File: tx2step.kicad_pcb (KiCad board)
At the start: 2 copper layers, 86.4 x 31.8 mm, 64 parts, among them CON1 BARREL_JACK, IC1 TPS2113A, IC2 MCP73831, IC3 TPS61202, IC4 DRV8834, IC5 DRV8834, J1 Prog, J2 8P8C, J3 CHASSIS_SWITCHES, J4 6P4Cx2, SW1 SW_DIP_x02, U1 ATmega328P-MMH, Y1 16 MHz

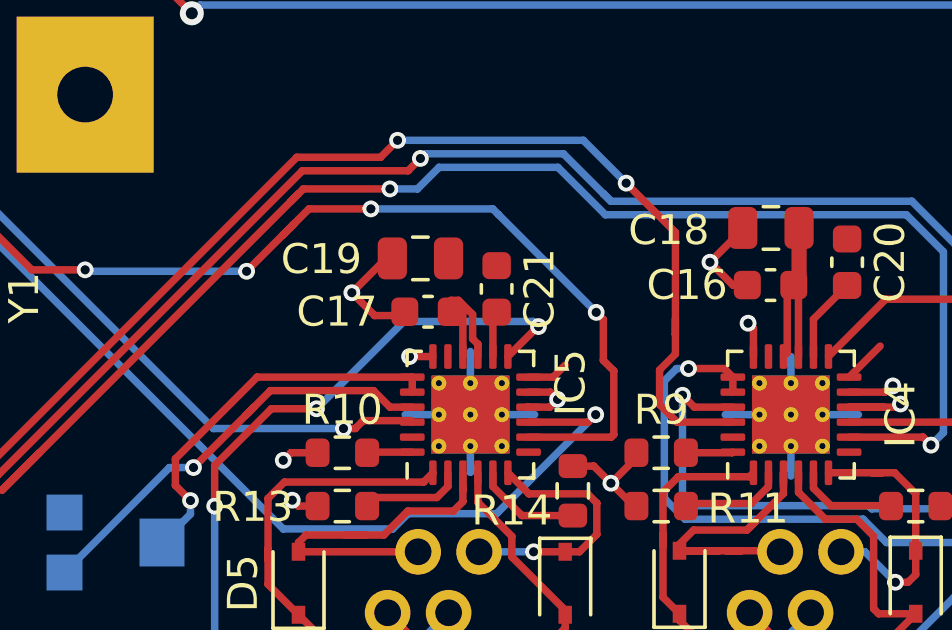
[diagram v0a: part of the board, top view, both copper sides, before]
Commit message: Restore capacitors on DRV8834 VINT
This pin still needs a capacitor even if it's not being used to
supply the CONFIG pin.
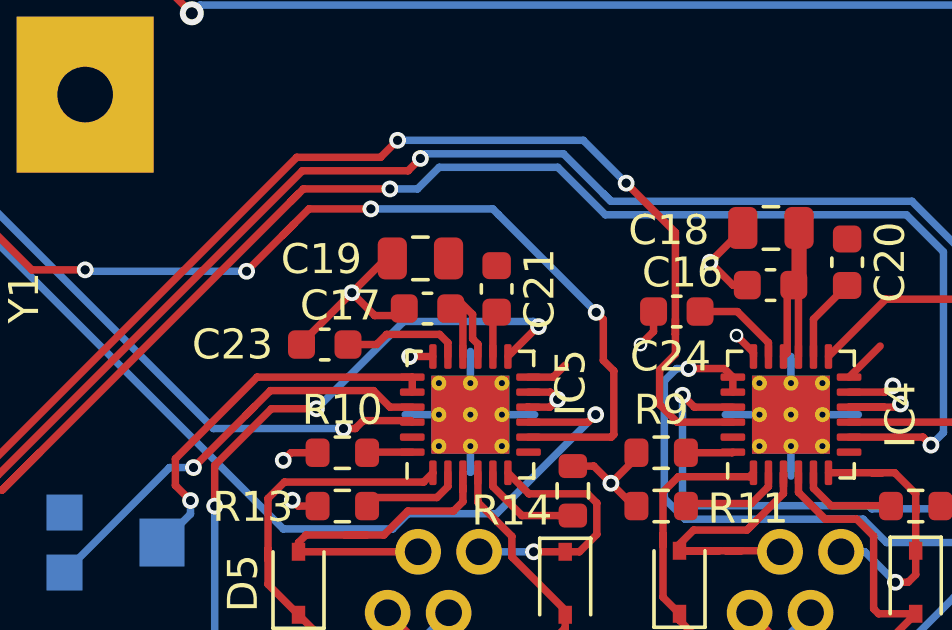
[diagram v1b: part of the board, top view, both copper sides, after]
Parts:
- added C23: 2.2 µF, Capacitor_SMD:C_0603_1608Metric, F.Cu at (140.6, 69.8)
- added C24: 2.2 µF, Capacitor_SMD:C_0603_1608Metric, F.Cu at (152.3, 68.7)
- moved C17 0.11 mm to (144.0, 68.6)
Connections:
- IC4 pad 17: (no net) -> Net-(C24-Pad2)
- IC4 pad 23: (no net) -> Net-(IC4-Pad23)
- IC4 pad 7: (no net) -> Net-(IC4-Pad7)
- IC5 pad 17: (no net) -> Net-(C23-Pad2)
- IC5 pad 23: (no net) -> Net-(IC5-Pad23)
- IC5 pad 7: (no net) -> Net-(IC5-Pad7)
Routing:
- net Net-(C23-Pad2): track 0.00 -> 4.05 mm
- net GND: track 102.9 -> 106.3 mm, vias 46 -> 47
- net Net-(C24-Pad2): track 0.00 -> 3.17 mm

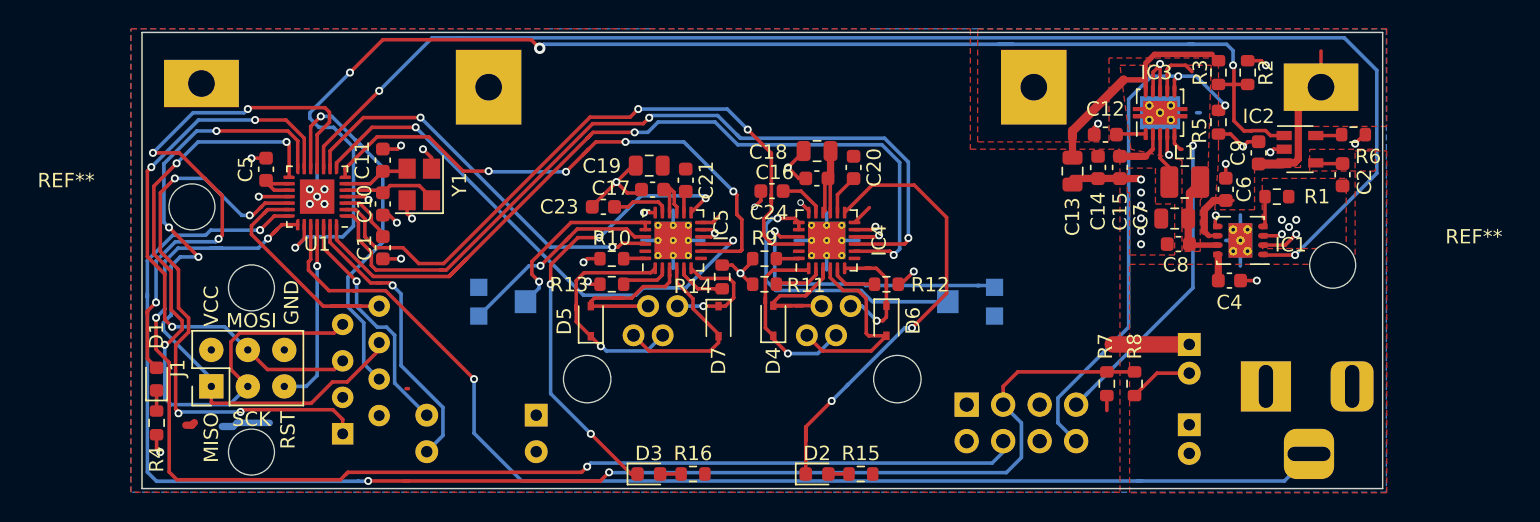
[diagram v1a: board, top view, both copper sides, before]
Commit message: Delete driver error LEDs
They don't actually seem particularly useful
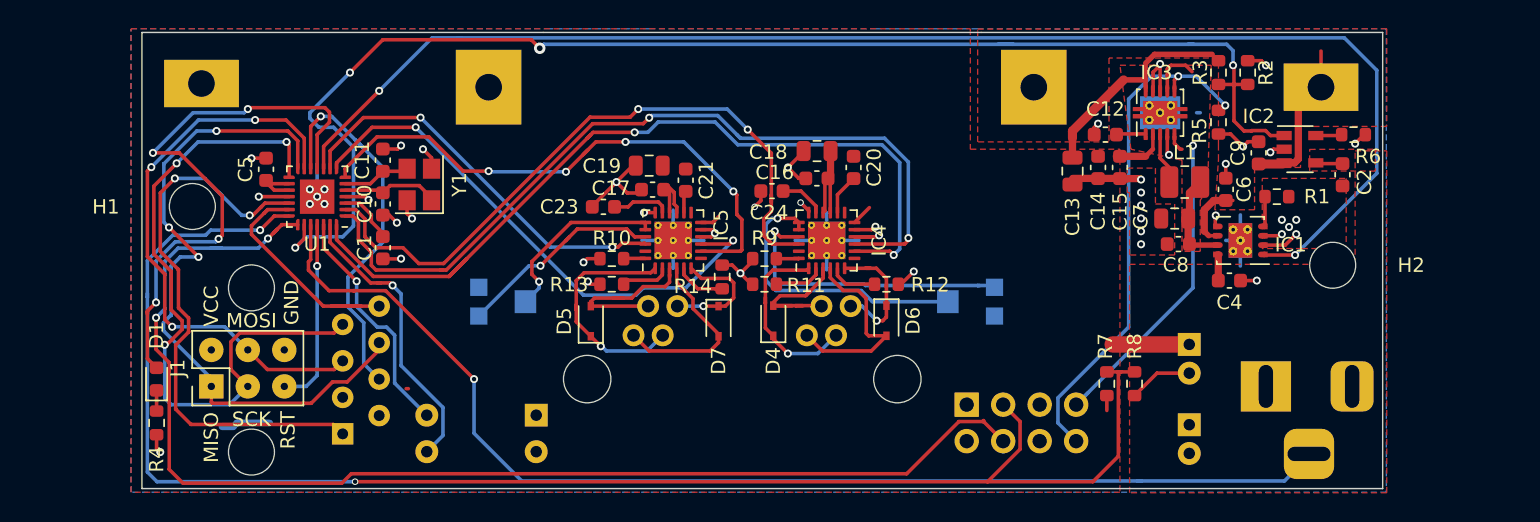
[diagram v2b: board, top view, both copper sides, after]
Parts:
- removed D2: ERR_RA, LED_SMD:LED_0603_1608Metric
- removed D3: ERR_DEC, LED_SMD:LED_0603_1608Metric
- removed R15, R16: 470Ω, Resistor_SMD:R_0603_1608Metric
- removed REF** (x2): MountingHole_3.2mm_M3, MountingHole:MountingHole_3.2mm_M3
- added H1: MountingHole, MountingHole:MountingHole_3.2mm_M3, F.Cu at (112.0, 69.8)
- added H2: MountingHole, MountingHole:MountingHole_3.2mm_M3, F.Cu at (191.3, 73.9)
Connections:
- IC4 pad 13: Net-(D2-Pad1) -> (no net)
- IC4 pad 23: Net-(IC4-Pad23) -> (no net)
- IC4 pad 7: Net-(IC4-Pad7) -> (no net)
- IC5 pad 13: Net-(D3-Pad1) -> (no net)
- IC5 pad 23: Net-(IC5-Pad23) -> (no net)
- IC5 pad 7: Net-(IC5-Pad7) -> (no net)
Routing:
- net Net-(D2-Pad1): track 32.6 -> 0.00 mm, vias 2 -> 0
- net Net-(D3-Pad1): track 31.6 -> 0.00 mm, vias 4 -> 0
- net /TRACK_RATE: track 103.3 -> 109.3 mm, vias 3 -> 2
- net Net-(D3-Pad2): track 1.46 -> 0.00 mm
- net /GUIDE_RATE: track 86.8 -> 88.2 mm, vias 3 -> 2
- net Net-(D2-Pad2): track 1.44 -> 0.00 mm
- net /JS_RA: track 40.6 -> 39.8 mm, vias 4 -> 2
- net VCC: track 48.8 -> 48.2 mm

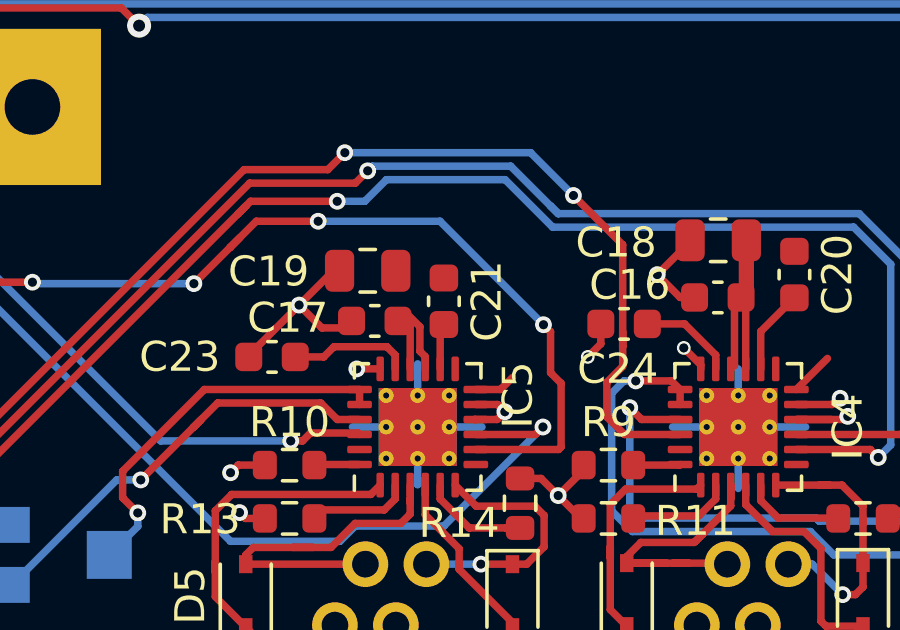
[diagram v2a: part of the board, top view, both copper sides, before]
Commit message: fix minor clearance issues
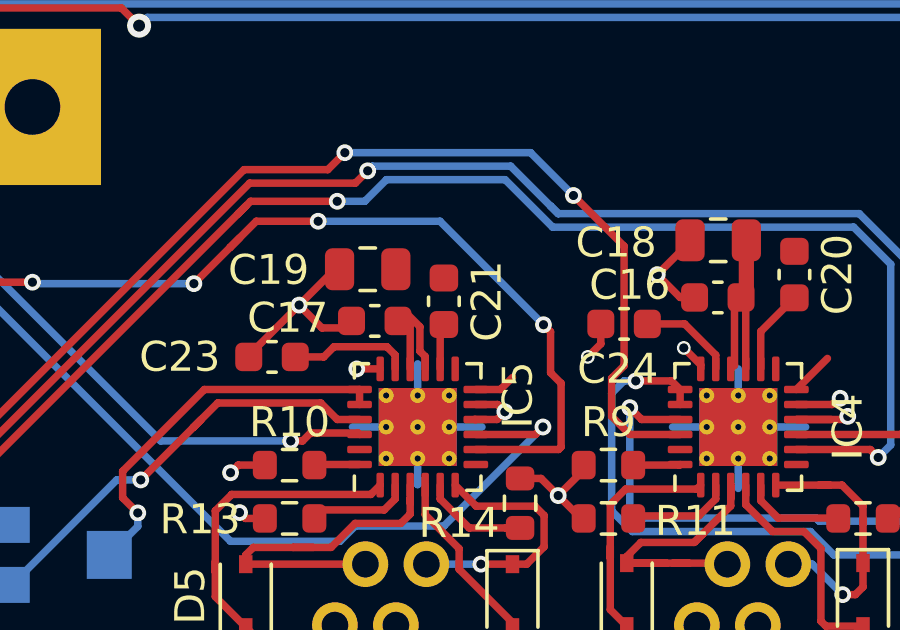
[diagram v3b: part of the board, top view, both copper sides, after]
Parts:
- moved C19 0.05 mm to (143.8, 66.9)
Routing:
- net /RA_PWR: track 46.8 -> 46.1 mm
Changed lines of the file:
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@@
     (thickness 1.6)
     (drawings 36)
-    (tracks 874)
+    (tracks 872)
     (zones 0)
     (modules 62)
@@
   )
   (module Capacitor_SMD:C_0805_2012Metric (layer F.Cu)
-    (at 143.764 66.929 180)
+    (at 143.764 66.8782 180)
     (descr "Capacitor SMD 0805 (2012 Metric), square (rectangular) end terminal, IPC_7351 nominal, (Body size source: https://docs.google.com/spreadsheets/d/1BsfQQcO9C6DZCsRaXUlFlo91Tg2WpOkGARC1WS5S8t0/edit?usp=sharing), generated with kicad-footprint-generator")
     (tags capacitor)
@@
   (via (at 143.002 62.992) (size 0.5588) (drill 0.3048) (layers F.Cu B.Cu) (net 23))
   (segment (start 143.002 62.992) (end 149.1944 62.992) (width 0.25) (layer B.Cu) (net 23))
-  (segment (start 154.178 72.386) (end 152.32241 72.386) (width 0.25) (layer F.Cu) (net 23) (status 10))
-  (segment (start 152.32241 72.386) (end 151.73641 71.8) (width 0.25) (layer F.Cu) (net 23))
-  (segment (start 151.73641 70.646104) (end 152.26359 70.118924) (width 0.25) (layer F.Cu) (net 23))
-  (segment (start 151.73641 71.8) (end 151.73641 70.646104) (width 0.25) (layer F.Cu) (net 23))
   (segment (start 143.002 62.992) (end 142.43601 63.55799) (width 0.25) (layer F.Cu) (net 23))
   (segment (start 142.43601 63.55799) (end 139.642009 63.557991) (width 0.25) (layer F.Cu) (net 23))
   (via (at 150.622 64.4196) (size 0.5588) (drill 0.3048) (layers F.Cu B.Cu) (net 23))
   (segment (start 149.1944 62.992) (end 150.622 64.4196) (width 0.25) (layer B.Cu) (net 23))
-  (segment (start 150.622 64.4196) (end 152.26359 66.06119) (width 0.25) (layer F.Cu) (net 23))
-  (segment (start 152.26359 66.06119) (end 152.26359 69.45959) (width 0.25) (layer F.Cu) (net 23))
-  (segment (start 152.26359 70.118924) (end 152.26359 69.45959) (width 0.25) (layer F.Cu) (net 23))
-  (segment (start 152.26359 69.45959) (end 152.26359 68.95159) (width 0.25) (layer F.Cu) (net 23))
   (segment (start 139.642009 63.557991) (end 129.456 73.744) (width 0.25) (layer F.Cu) (net 23))
   (segment (start 129.456 73.744) (end 127.724514 73.744) (width 0.25) (layer F.Cu) (net 23))
   (segment (start 126.624514 72.644) (end 124.744166 72.644) (width 0.25) (layer F.Cu) (net 23))
   (segment (start 127.724514 73.744) (end 126.624514 72.644) (width 0.25) (layer F.Cu) (net 23))
+  (segment (start 152.501086 72.386) (end 154.178 72.386) (width 0.25) (layer F.Cu) (net 23))
+  (segment (start 151.895599 71.780513) (end 152.501086 72.386) (width 0.25) (layer F.Cu) (net 23))
+  (segment (start 151.895599 70.509887) (end 151.895599 71.780513) (width 0.25) (layer F.Cu) (net 23))
+  (segment (start 152.31 70.095486) (end 151.895599 70.509887) (width 0.25) (layer F.Cu) (net 23))
+  (segment (start 152.31 66.1076) (end 152.31 70.095486) (width 0.25) (layer F.Cu) (net 23))
+  (segment (start 150.622 64.4196) (end 152.31 66.1076) (width 0.25) (layer F.Cu) (net 23))
   (segment (start 143.4925 71.386) (end 143.4925 70.886) (width 0.25) (layer F.Cu) (net 24) (status 30))
   (via (at 136.1 75) (size 0.5588) (drill 0.3048) (layers F.Cu B.Cu) (net 24))

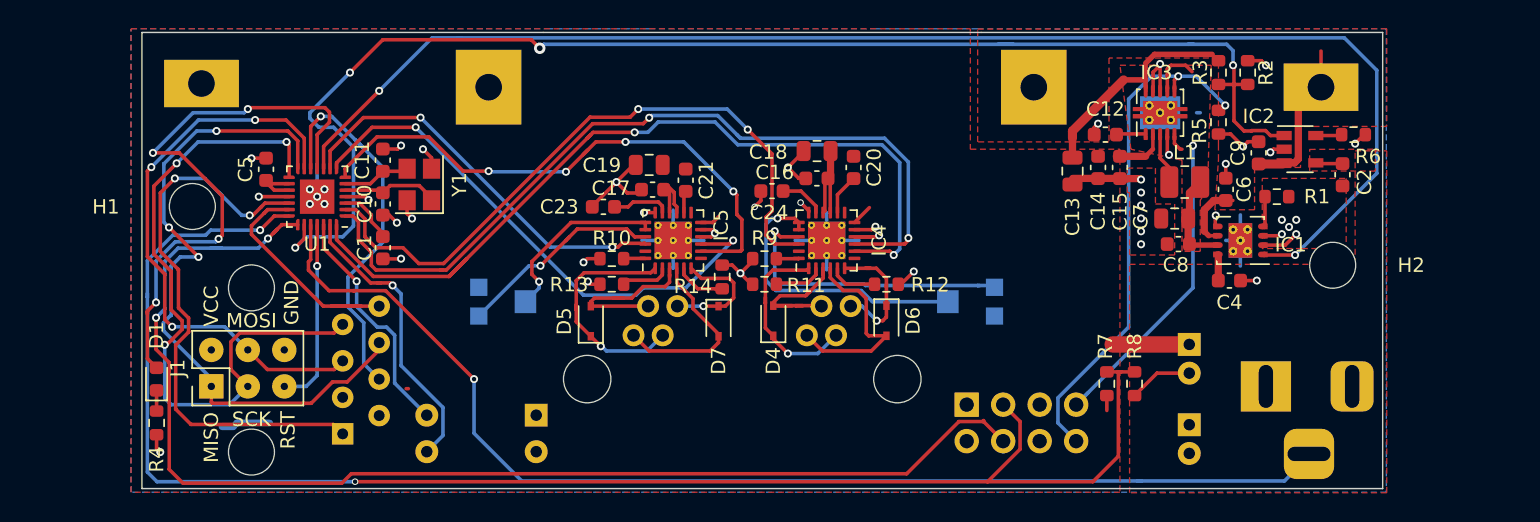
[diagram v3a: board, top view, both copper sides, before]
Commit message: Replace MCP73831 and TPS2113A with MCP73871
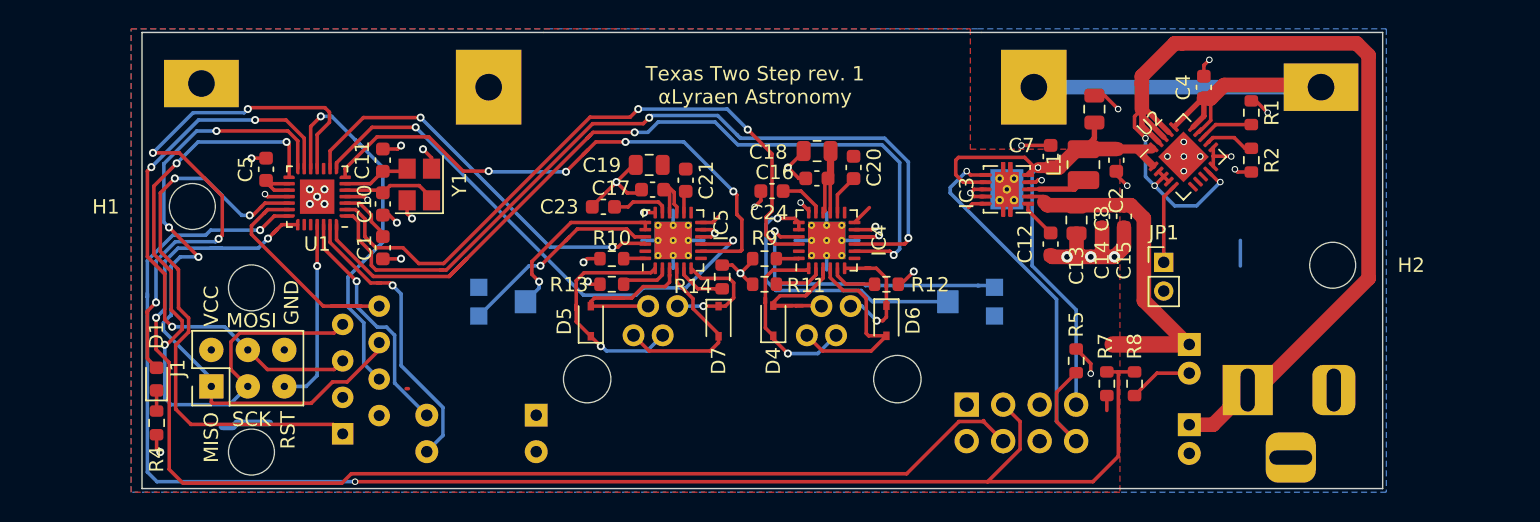
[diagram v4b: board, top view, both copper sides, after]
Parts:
- removed C6: 1µF, Capacitor_SMD:C_0603_1608Metric
- removed C9: 4.7µF, Capacitor_SMD:C_0603_1608Metric
- removed IC1: TPS2113A, Package_SON:Texas_S-PVSON-N8_ThermalVias
- removed IC2: MCP73831, Package_TO_SOT_SMD:SOT-23-5
- removed R3: 10KΩ, Resistor_SMD:R_0603_1608Metric
- removed R6: 2KΩ, Resistor_SMD:R_0603_1608Metric
- added JP1: THERM, Connector_PinHeader_2.00mm:PinHeader_1x02_P2.00mm_Vertical, F.Cu at (179.6, 73.7)
- added U2: MCP73871-2AA, Package_DFN_QFN:QFN-20-1EP_4x4mm_P0.5mm_EP2.5x2.5mm, F.Cu at (180.9, 66.3)
- BT1: value LiIon 18650 -> LiIon 21700
- C4: value 1µF -> 4.7µF
- R1: value 470Ω -> 1KΩ
- moved R5 19.3 mm to (173.5, 80.5), turned to 90 degrees
- moved C2 15.8 mm to (176.3, 66.5)
- moved C4 13.6 mm to (182.4, 61.5), turned to 90 degrees
- moved IC3 11.9 mm to (168.7, 68.6), turned to 180 degrees
- moved C7 10.8 mm to (171.7, 66.3), turned to 90 degrees
- moved C8 9.45 mm to (174.8, 63.0), turned to 90 degrees
- moved C12 8.52 mm to (171.7, 72.4), turned to 270 degrees
- moved L1 7.16 mm to (174.0, 66.9), turned to 90 degrees
- moved R2 6.51 mm to (185.7, 66.5)
- moved R1 6.11 mm to (185.7, 63.2), turned to 270 degrees
- moved C14 3.42 mm to (175.3, 70.5)
- moved C15 3.42 mm to (176.8, 70.5)
- moved C13 3.42 mm to (173.5, 70.7)
- moved CON1 1.30 mm to (185.4, 82.5)
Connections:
- C2 pad 1: +5V -> /REG_IN
- C4 pad 1: +5V -> Net-(BT1-Pad1)
- CON1 pad 3: /DC_SENSE -> (no net)
- R1 pad 1: Net-(IC1-Pad4) -> GND
- R1 pad 2: GND -> Net-(R1-Pad2)
- R2 pad 1: VCC -> Net-(R2-Pad1)
- R2 pad 2: /CHARGE_STAT -> GND
- U1 pad 10: /MUX_STAT -> (no net)
- U1 pad 23: /CHARGE_STAT -> (no net)
- U1 pad 24: /DC_SENSE -> (no net)
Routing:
- net /MUX_STAT: track 96.6 -> 0.00 mm, vias 2 -> 0
- net /CHARGE_STAT: track 96.0 -> 0.00 mm, vias 4 -> 0
- net /DC_SENSE: track 82.4 -> 0.00 mm, vias 1 -> 0
- net +5V: track 4.07 -> 74.5 mm, vias 0 -> 3
- net Net-(BT1-Pad1): track 20.0 -> 42.3 mm
- net /REG_IN: track 34.6 -> 41.8 mm
- net /SW_POWER: track 36.5 -> 30.2 mm, vias 2 -> 1
- net Net-(JP1-Pad1): track 0.00 -> 5.56 mm
- net Net-(R1-Pad2): track 0.00 -> 3.72 mm
- net Net-(R2-Pad1): track 0.00 -> 3.50 mm
- net Net-(IC1-Pad4): track 2.14 -> 0.00 mm
- net GND: track 106.3 -> 104.4 mm, vias 47 -> 44
- net Net-(IC2-Pad5): track 1.83 -> 0.00 mm
- net Net-(IC3-Pad3): track 2.60 -> 4.13 mm
- net Net-(C12-Pad1): track 2.06 -> 2.69 mm
- removed copper zone on F.Cu, net +5V
- removed copper zone on F.Cu, net /REG_IN
- removed copper zone on F.Cu, net GND
- removed copper zone on F.Cu, net Net-(BT1-Pad1)
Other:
- board text added: "Texas Two Step rev. 1 αLyraen Astronomy"
- board text removed: "Texas Two Step rev. 0.2 αLyraen Astronomy"
